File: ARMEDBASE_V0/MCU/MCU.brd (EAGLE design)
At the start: 160 x 100 mm, 35 parts, among them IC1 REG1117, IC2 MEGA8-P, K1 CQ1-12V, Q1 20Mhz, Q2 2N3904, Q3 2N3904

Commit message: 7805
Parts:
- removed IC1: REG1117, burr-brown:SOT223
- added IC3: (no value), SparkFun-PowerIC:TO-220-ALT
- added X1: (no value), con-berg:PN87520
- moved K1 95.2 mm to (146.1, 34.3)
- moved R11 15.7 mm to (64.8, 87.6), turned to 0 degrees
- moved Q3 13.5 mm to (57.1, 82.5), turned to 180 degrees
- moved D2 13.0 mm to (58.4, 87.6), turned to 180 degrees
- moved C3 11.4 mm to (16.5, 50.8)
- moved S2 8.98 mm to (6.35, 73.7)
- moved S1 8.89 mm to (6.35, 81.3)
- moved Q1 7.62 mm to (22.9, 50.8)
- moved C4 7.62 mm to (16.5, 47.0)
- moved IC2 7.62 mm to (36.8, 52.1)
- moved C5 3.81 mm to (16.5, 54.6)
- moved R7 3.81 mm to (49.5, 80.0)
- moved R4 2.84 mm to (38.1, 80.0)
- moved R5 2.84 mm to (41.9, 80.0)
- moved R6 2.84 mm to (45.7, 80.0)
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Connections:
- removed net N$1: J2.2, K1.NO
- net GND: now also IC3.GND; no longer IC1.1, K1.C
- net N$5: now also J2.1; no longer K1.1
- net VCC12V: now also IC3.IN, J2.2; no longer IC1.3, J2.1, K1.2
- net VCC5V: now also IC3.OUT; no longer IC1.2
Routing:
- net TX: track 91.3 -> 42.0 mm, vias 0 -> 1
- net VCC12V: track 116.4 -> 157.6 mm
- net VCC5V: track 166.7 -> 132.4 mm, vias 0 -> 2
- net N$9: track 41.1 -> 68.8 mm
- net RX: track 26.4 -> 44.4 mm
- net N$6: track 4.54 -> 20.8 mm
- net GND: track 253.5 -> 269.4 mm, vias 0 -> 1
- net VCC: track 24.9 -> 11.6 mm
- net N$24: track 72.5 -> 82.6 mm
- net N$2: track 10.7 -> 19.9 mm, vias 0 -> 1
- net N$1: track 8.96 -> 0.00 mm
- net N$13: track 17.4 -> 8.54 mm
- net N$4: track 26.6 -> 32.4 mm
- net N$21: track 30.4 -> 24.6 mm
- net N$8: track 35.1 -> 39.4 mm, vias 0 -> 1
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
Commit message: usb
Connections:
- net GND: now also X1.4
- net VCC5V: now also X1.1
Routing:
- net VCC5V: track 132.4 -> 186.9 mm
- net GND: track 269.4 -> 303.4 mm
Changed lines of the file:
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@@
 <via x="13.97" y="69.85" extent="1-16" drill="0.6096"/>
 <via x="49.53" y="85.09" extent="1-16" drill="0.6096"/>
+<contactref element="X1" pad="1"/>
+<wire x1="41.91" y1="48.26" x2="78.74" y2="85.09" width="0.254" layer="16"/>
+<wire x1="40.64" y1="48.26" x2="41.91" y2="48.26" width="0.254" layer="16"/>
+<wire x1="78.74" y1="85.09" x2="78.43" y2="86.19" width="0.254" layer="16"/>
 </signal>
 <signal name="GND">
@@
 <wire x1="45.72" y1="76.2" x2="46.99" y2="77.47" width="0.254" layer="16"/>
 <wire x1="10.16" y1="76.2" x2="15.24" y2="76.2" width="0.254" layer="16"/>
-<wire x1="15.24" y1="76.2" x2="45.72" y2="76.2" width="0.254" layer="16"/>
+<wire x1="15.24" y1="76.2" x2="41.91" y2="76.2" width="0.254" layer="16"/>
+<wire x1="41.91" y1="76.2" x2="45.72" y2="76.2" width="0.254" layer="16"/>
 <wire x1="48.26" y1="80.01" x2="48.63" y2="80.01" width="0.254" layer="1"/>
 <wire x1="10.16" y1="76.2" x2="9.6012" y2="75.9206" width="0.254" layer="16"/>
@@
 <wire x1="8.89" y1="76.2" x2="9.6012" y2="75.9206" width="0.254" layer="1"/>
 <via x="46.99" y="77.47" extent="1-16" drill="0.6096"/>
+<contactref element="X1" pad="4"/>
+<wire x1="66.04" y1="80.01" x2="71.12" y2="85.09" width="0.254" layer="16"/>
+<wire x1="45.72" y1="80.01" x2="66.04" y2="80.01" width="0.254" layer="16"/>
+<wire x1="41.91" y1="76.2" x2="45.72" y2="80.01" width="0.254" layer="16"/>
+<wire x1="71.12" y1="85.09" x2="71.43" y2="86.19" width="0.254" layer="16"/>
 </signal>
 <signal name="N$11">

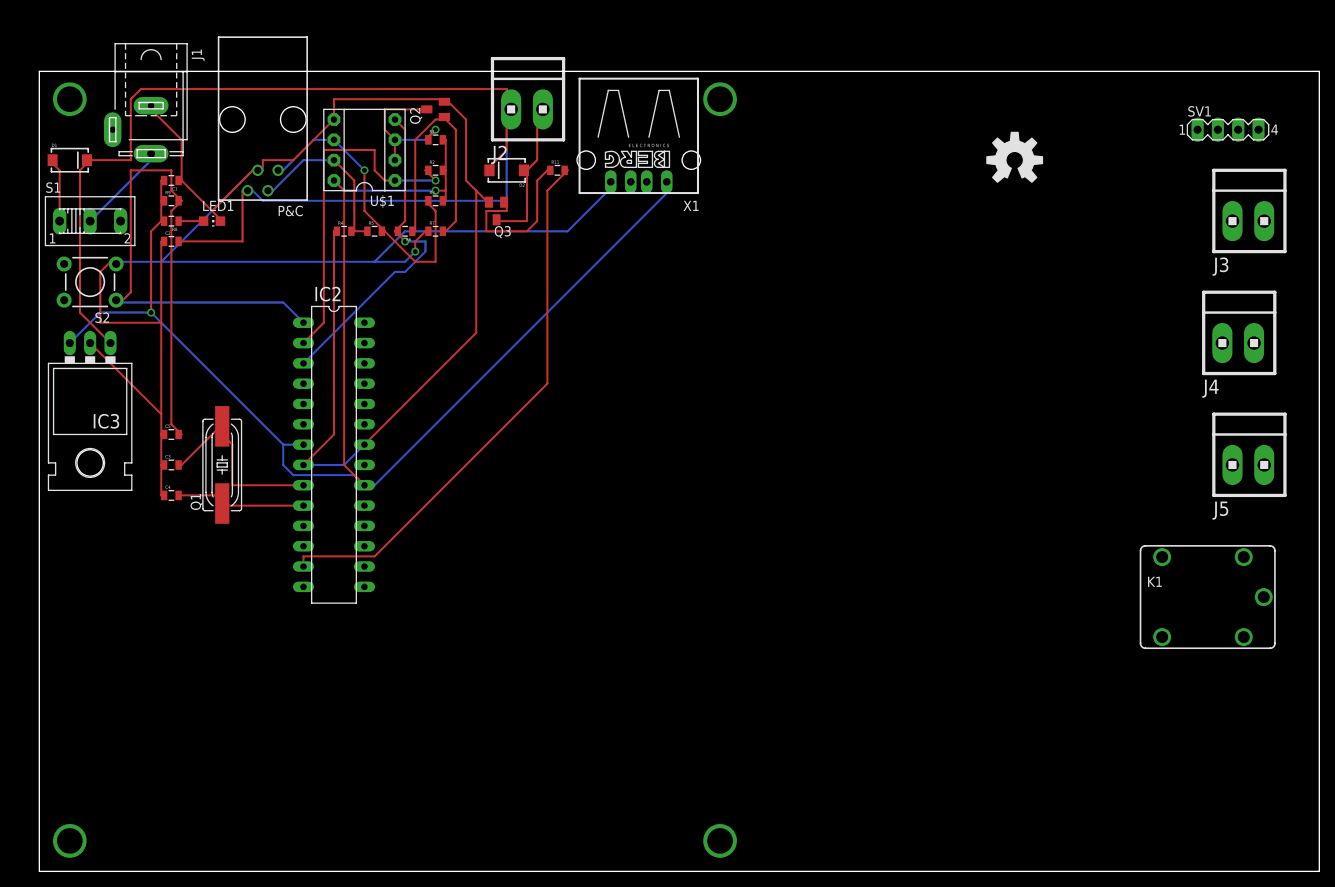
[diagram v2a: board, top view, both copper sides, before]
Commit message: modbus in-out
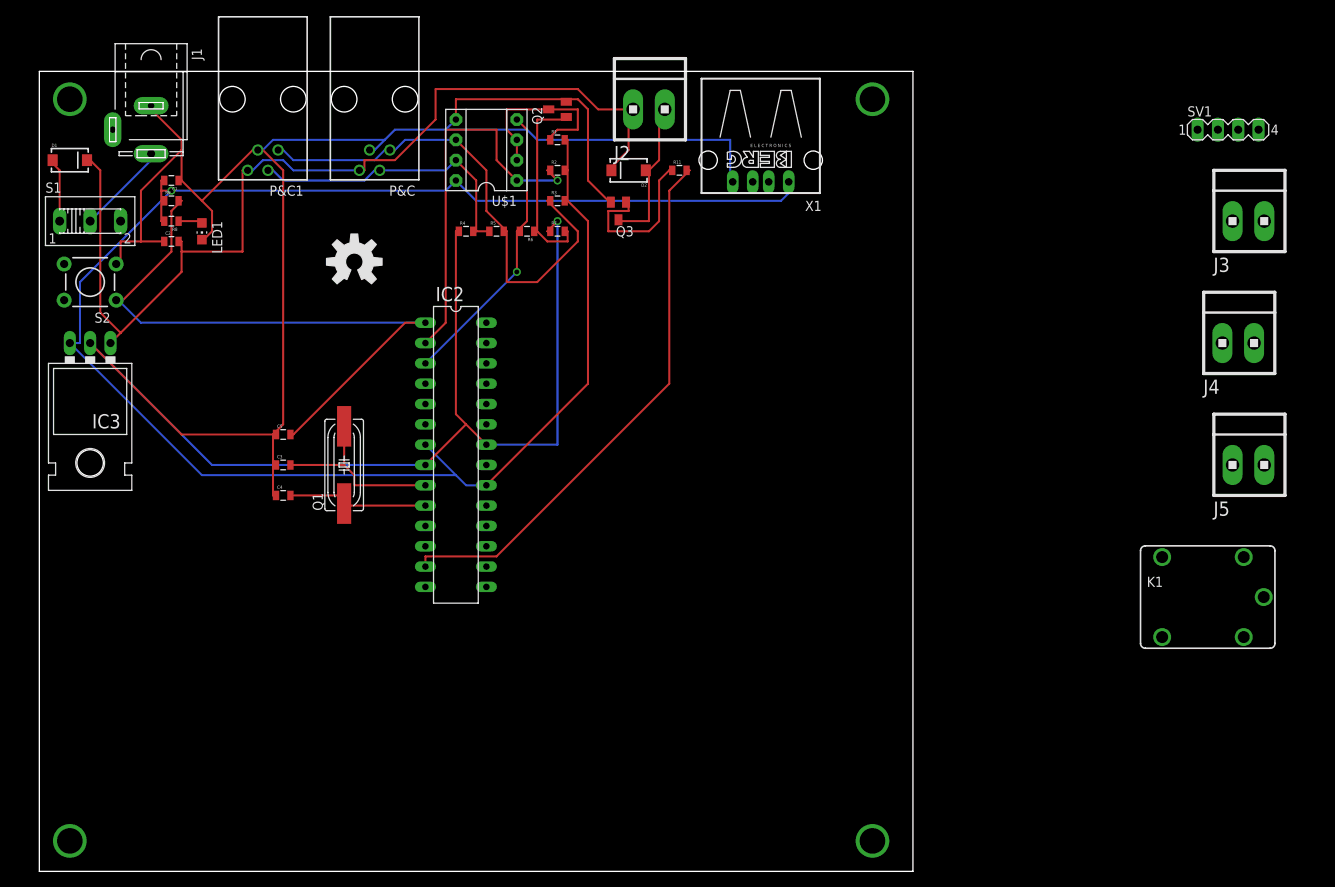
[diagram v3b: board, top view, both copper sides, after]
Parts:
- added P&C1: 14867, con-4ucon:14867
- moved LOGO1 83.5 mm to (39.4, 76.2)
- moved R11 15.2 mm to (80.0, 87.6)
- moved IC2 15.2 mm to (52.1, 52.1)
- moved J2 15.2 mm to (76.2, 95.2)
- moved Q1 15.2 mm to (38.1, 50.8)
- moved Q3 15.2 mm to (72.4, 82.5)
- moved R4 15.2 mm to (53.3, 80.0)
- moved R5 15.2 mm to (57.1, 80.0)
- moved R6 15.2 mm to (61.0, 80.0)
- moved U$1 15.2 mm to (55.9, 90.2)
- moved D2 15.2 mm to (73.7, 87.6)
- moved Q2 15.2 mm to (64.8, 95.2)
- moved R1 15.2 mm to (64.8, 91.4)
- moved R2 15.2 mm to (64.8, 87.6)
- moved R3 15.2 mm to (64.8, 83.8)
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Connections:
- net GND: now also P&C1.3
- net N$7: now also P&C1.2
- net N$8: now also P&C1.1
- net VCC12V: now also P&C1.4
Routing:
- net GND: track 303.4 -> 353.2 mm
- net VCC5V: track 186.9 -> 228.7 mm, vias 2 -> 1
- net VCC12V: track 157.6 -> 125.3 mm
- net N$8: track 39.4 -> 62.6 mm, vias 1 -> 0
- net N$7: track 21.8 -> 37.0 mm
- net N$4: track 32.4 -> 24.5 mm
- net TX: track 42.0 -> 36.6 mm
- net RX: track 44.4 -> 48.7 mm
- net N$24: track 82.6 -> 79.3 mm
- net N$2: track 19.9 -> 23.0 mm, vias 1 -> 0
- net N$23: track 16.9 -> 18.2 mm
- net N$21: track 24.6 -> 23.5 mm
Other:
- board size 160 x 100 mm -> 109.2 x 100 mm

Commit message: arg
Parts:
- moved IC2 12.8 mm to (39.4, 50.8)
- moved Q1 12.8 mm to (25.4, 49.5)
- moved C3 12.8 mm to (17.8, 49.5)
- moved C4 12.8 mm to (17.8, 45.7)
- moved C5 12.8 mm to (17.8, 53.3)
- moved D1 12.0 mm to (14.0, 82.5)
- moved LED1 10.2 mm to (19.1, 69.8), turned to 270 degrees
- moved C1 10.2 mm to (21.6, 77.5)
- moved R8 7.73 mm to (17.8, 73.7)
- moved C2 7.18 mm to (21.6, 73.7)
- moved R9 6.48 mm to (17.8, 77.5), turned to 180 degrees
- moved S1 6.35 mm to (2.54, 86.4), turned to 90 degrees
- moved IC3 2.84 mm to (7.62, 59.7)
- moved S2 1.27 mm to (6.35, 74.9)
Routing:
- net GND: track 353.2 -> 312.8 mm
- net VCC5V: track 228.7 -> 207.7 mm, vias 1 -> 0
- net N$24: track 79.3 -> 60.2 mm
- net TX: track 36.6 -> 48.4 mm
- net VCC12V: track 125.3 -> 118.6 mm
- net RX: track 48.7 -> 42.1 mm
- net N$9: track 68.8 -> 75.3 mm
- net N$8: track 62.6 -> 59.8 mm
- net N$11: track 3.13 -> 4.93 mm
- net N$4: track 24.5 -> 26.3 mm
- net VCC: track 11.6 -> 13.3 mm
- net N$13: track 8.54 -> 9.28 mm

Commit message: MCU almost
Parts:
- removed J3, J4, J5: (no value), con-amp:1X2MTA
- removed K1: CQ1-12V, relay:CQ1
- added F1: 1.5A, special:FUSE
- added SV2: (no value), con-lstb:MA08-1
- added SV3, SV5: 5v, con-lstb:MA04-1
- added SV4: (no value), con-lstb:MA07-1
- Q1: value 20Mhz -> 16Mhz
- moved SV1 124.8 mm to (59.7, 5.08)
- moved R3 47.7 mm to (33.0, 48.3), turned to 180 degrees
- moved U$1 42.2 mm to (61.0, 48.3)
- moved R11 40.7 mm to (77.5, 47.0)
- moved R1 39.7 mm to (69.8, 52.1)
- moved R2 39.7 mm to (69.8, 48.3)
- moved X1 39.1 mm to (58.4, 66.0)
- moved Q2 38.3 mm to (68.6, 57.1), turned to 0 degrees
- moved R4 37.8 mm to (27.9, 52.1)
- moved R5 36.9 mm to (33.0, 52.1)
- moved LOGO1 35.8 mm to (29.2, 41.9)
- moved Q3 30.9 mm to (77.5, 52.1), turned to 0 degrees
- moved C5 30.7 mm to (48.3, 49.5), turned to 270 degrees
- moved D1 30.7 mm to (10.2, 52.1)
- moved J2 30.6 mm to (78.7, 64.8)
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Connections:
- new net KP1: IC2.24, SV4.1
- new net KP2: IC2.23, SV4.2
- new net KP3: IC2.19, SV4.3
- new net KP4: IC2.16, SV4.4
- new net KP5: IC2.15, SV4.5
- new net KP6: IC2.14, SV4.6
- new net KP7: IC2.12, SV4.7
- new net LCDD4: IC2.11, SV3.4
- new net LCDD5: IC2.6, SV3.3
- new net LCDD6: IC2.5, SV3.2
- new net LCDD7: IC2.4, SV3.1
- new net LCDEN: IC2.17, SV2.1
- new net LCDRS: IC2.18, SV2.3
- new net N$1: C1.2, F1.1, IC3.OUT, R8.2
- new net N$15: IC2.25, SV1.1
- new net N$16: IC2.26, SV1.2
- new net N$17: IC2.27, SV1.3
- new net N$18: IC2.28, SV1.4
- net GND: now also SV2.2, SV2.4, SV2.6, SV5.1, SV5.2
- net VCC12V: now also SV5.4
- net VCC5V: now also F1.2, SV2.5, SV5.3; no longer C1.2, IC3.OUT, R8.2
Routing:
- net N$1: track 0.00 -> 55.6 mm
- net VCC12V: track 118.6 -> 173.1 mm
- net KP1: track 0.00 -> 46.3 mm
- net LCDRS: track 0.00 -> 39.7 mm, vias 0 -> 1
- net KP3: track 0.00 -> 38.0 mm
- net LCDEN: track 0.00 -> 37.9 mm
- net LCDD4: track 0.00 -> 35.3 mm
- net KP2: track 0.00 -> 35.1 mm
- net VCC5V: track 207.7 -> 241.5 mm
- net N$24: track 60.2 -> 93.1 mm, vias 0 -> 1
- net LCDD5: track 0.00 -> 32.4 mm
- net LCDD7: track 0.00 -> 23.0 mm, vias 0 -> 1
- net LCDD6: track 0.00 -> 23.0 mm, vias 0 -> 1
- net KP4: track 0.00 -> 21.7 mm
- net TX: track 48.4 -> 26.9 mm
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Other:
- board size 109.2 x 100 mm -> 99 x 69.5 mm
- board text added: "CLK ARMED BASE MCU"

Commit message: net class settings
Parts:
- moved LED1 14.0 mm to (19.1, 55.9)
- turned F1 to 180 degrees
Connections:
- net N$1: now also F1.2, IC3.IN; no longer C1.2, F1.1, IC3.OUT, R8.2
- net VCC12V: now also F1.1; no longer IC3.IN
- net VCC5V: now also C1.2, IC3.OUT, R8.2; no longer F1.2
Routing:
- net GND: track 332.1 -> 280.0 mm, vias 1 -> 0
- net N$1: track 55.6 -> 29.1 mm
- net KP3: track 38.0 -> 24.1 mm, vias 0 -> 1
- net VCC12V: track 173.1 -> 162.4 mm
- net KP1: track 46.3 -> 36.6 mm
- net LCDD6: track 23.0 -> 32.6 mm, vias 1 -> 0
- net N$21: track 20.3 -> 28.7 mm, vias 0 -> 1
- net RX: track 24.6 -> 18.7 mm
- net N$11: track 4.93 -> 10.5 mm
- net KP4: track 21.7 -> 17.4 mm, vias 0 -> 1
- net VCC5V: track 241.5 -> 245.7 mm, vias 0 -> 2
- net N$8: track 50.1 -> 46.5 mm
- net N$24: track 93.1 -> 95.6 mm
- net LCDD5: track 32.4 -> 29.9 mm
- net TX: track 26.9 -> 29.3 mm, vias 1 -> 0
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
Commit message: WE
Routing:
- net VCC5V: track 245.7 -> 209.5 mm, vias 2 -> 3
- net LCDD7: track 20.8 -> 31.3 mm, vias 1 -> 0
- net LCDD6: track 32.6 -> 22.8 mm, vias 0 -> 1
- net VCC12V: track 162.4 -> 153.2 mm, vias 0 -> 1
- net N$24: track 95.6 -> 88.4 mm
- net GND: track 280.0 -> 273.2 mm, vias 0 -> 1
- net LCDD5: track 29.9 -> 23.7 mm, vias 0 -> 1
- net KP3: track 24.1 -> 23.9 mm, vias 1 -> 0

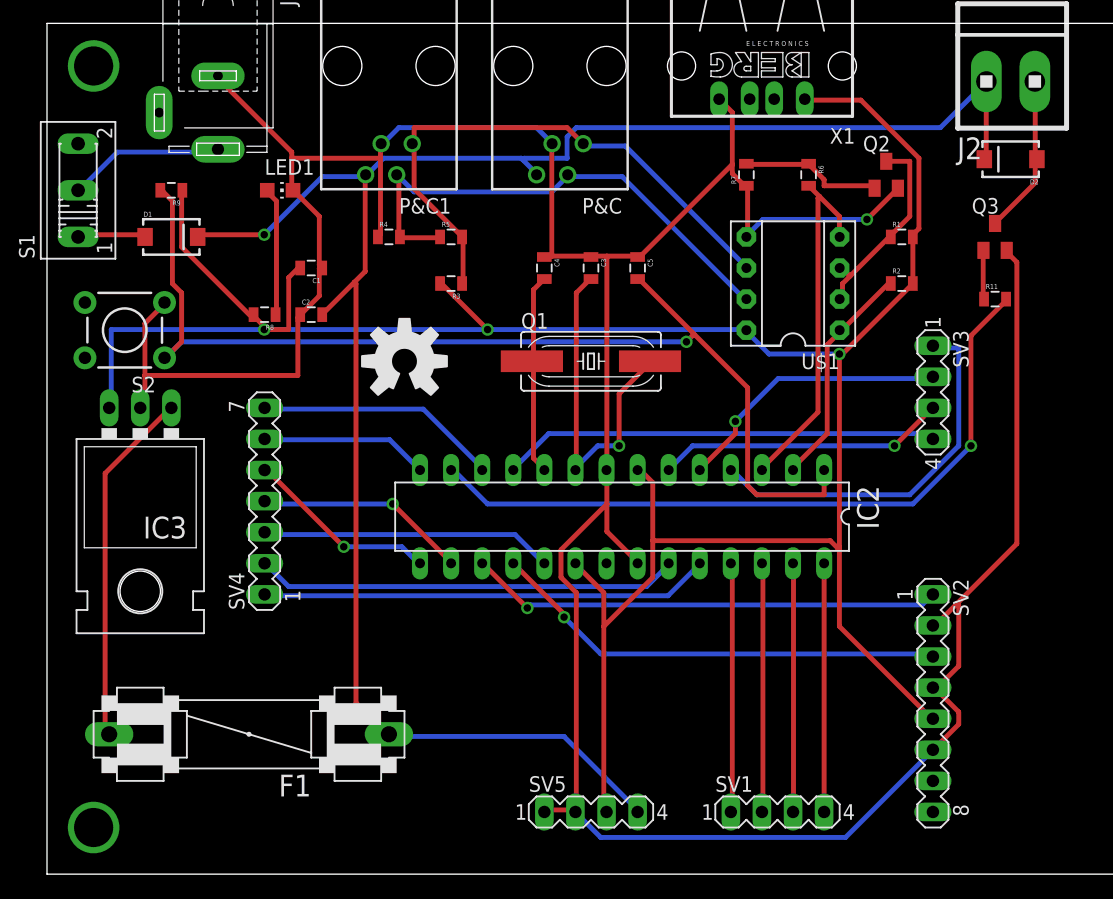
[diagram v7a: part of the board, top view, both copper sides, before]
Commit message: fuse replace
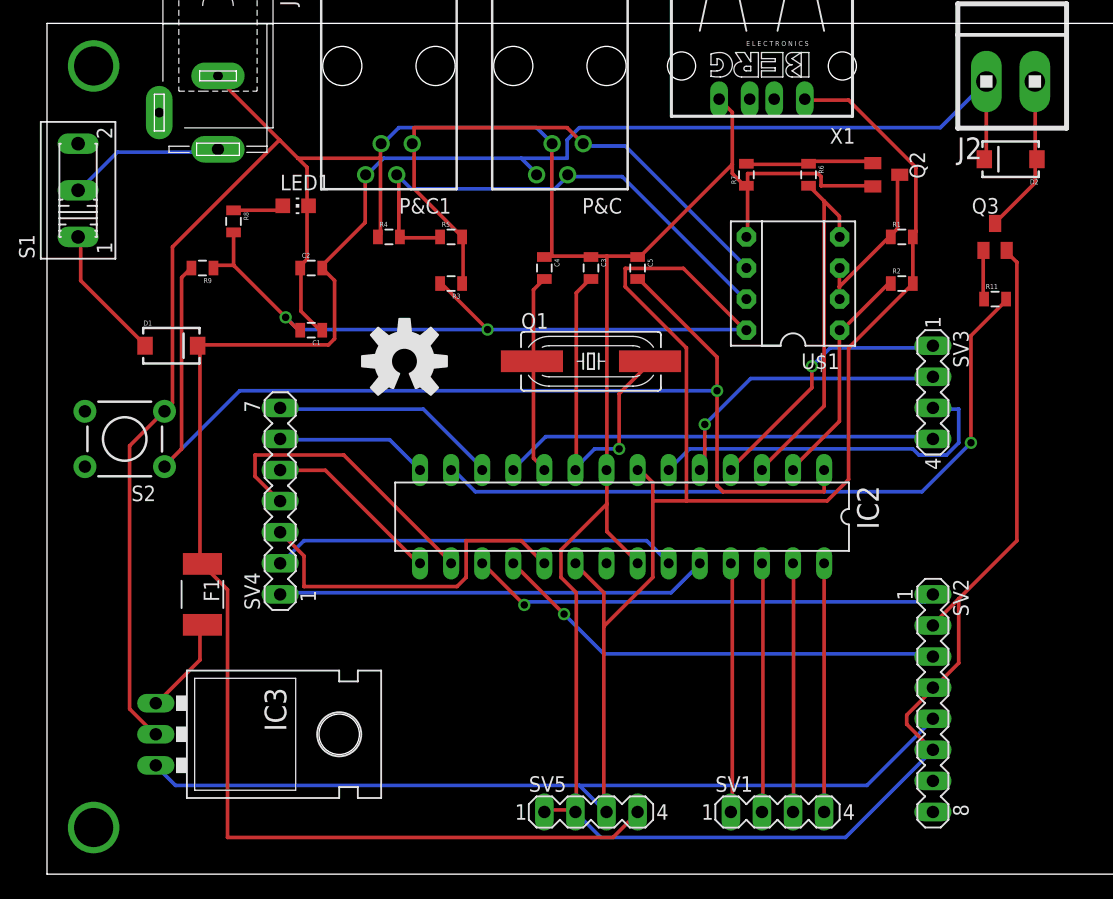
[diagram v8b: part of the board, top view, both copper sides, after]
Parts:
- F1: device special:FUSE -> _hhn_PtcFuses_Siba_r500_Ozan:1820
- moved IC3 23.4 mm to (12.7, 11.4), turned to 270 degrees
- moved F1 12.0 mm to (12.7, 22.9), turned to 270 degrees
- moved D1 8.89 mm to (10.2, 43.2)
- moved S2 8.89 mm to (6.35, 35.6)
- moved R8 8.03 mm to (15.2, 53.3), turned to 270 degrees
- moved R9 6.84 mm to (12.7, 49.5)
- moved C1 5.08 mm to (21.6, 44.5)
- moved C2 3.81 mm to (21.6, 49.5)
- moved LED1 1.80 mm to (20.3, 54.6)
- moved SV4 1.27 mm to (19.1, 30.5)
- turned Q2 to 270 degrees
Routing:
- net VCC5V: track 209.5 -> 250.5 mm, vias 3 -> 2
- net GND: track 273.2 -> 299.3 mm, vias 1 -> 0
- net N$1: track 29.1 -> 8.05 mm
- net VCC12V: track 153.2 -> 165.4 mm, vias 1 -> 0
- net LCDD7: track 31.3 -> 21.8 mm, vias 0 -> 1
- net KP4: track 17.4 -> 24.4 mm, vias 1 -> 0
- net N$24: track 88.4 -> 95.2 mm
- net LCDD5: track 23.7 -> 29.9 mm, vias 1 -> 0
- net N$11: track 10.5 -> 4.38 mm
- net N$13: track 5.71 -> 11.2 mm
- net KP3: track 23.9 -> 29.0 mm
- net N$2: track 16.8 -> 13.8 mm
- net KP1: track 36.7 -> 35.4 mm
- net KP2: track 34.6 -> 33.3 mm
- net LCDD6: track 22.8 -> 24.1 mm
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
